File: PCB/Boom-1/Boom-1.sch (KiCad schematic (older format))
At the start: 714 parts, among them U1 CEM3340, U10 AS3320, U11 AS3310, U12 AS3310, U13 AS3310, U14 AS3310, U15 V2164D, U16 AS3310, U17 AS3310, U18 V2164D, U19 TL074, U2 CEM3340, U20 TL074, U21 TL074, U22 TL074, U23 TL074, U24 TL074, U25 TL074, U26 TL074, U27 TL072, U28 TL074, U29 TL072, U3 4013, U30 TL074, U31 TL072, U32 TL074, U33 TL074, U34 TL074, U35 TL072, U36 TL074, U37 TL074, U38 TL072, U39 TL074, U4 NOISE, U40 TL072, U5 V2164D, U6 V2164D, U7 V2164D, U8 AS3320, U9 AS3320

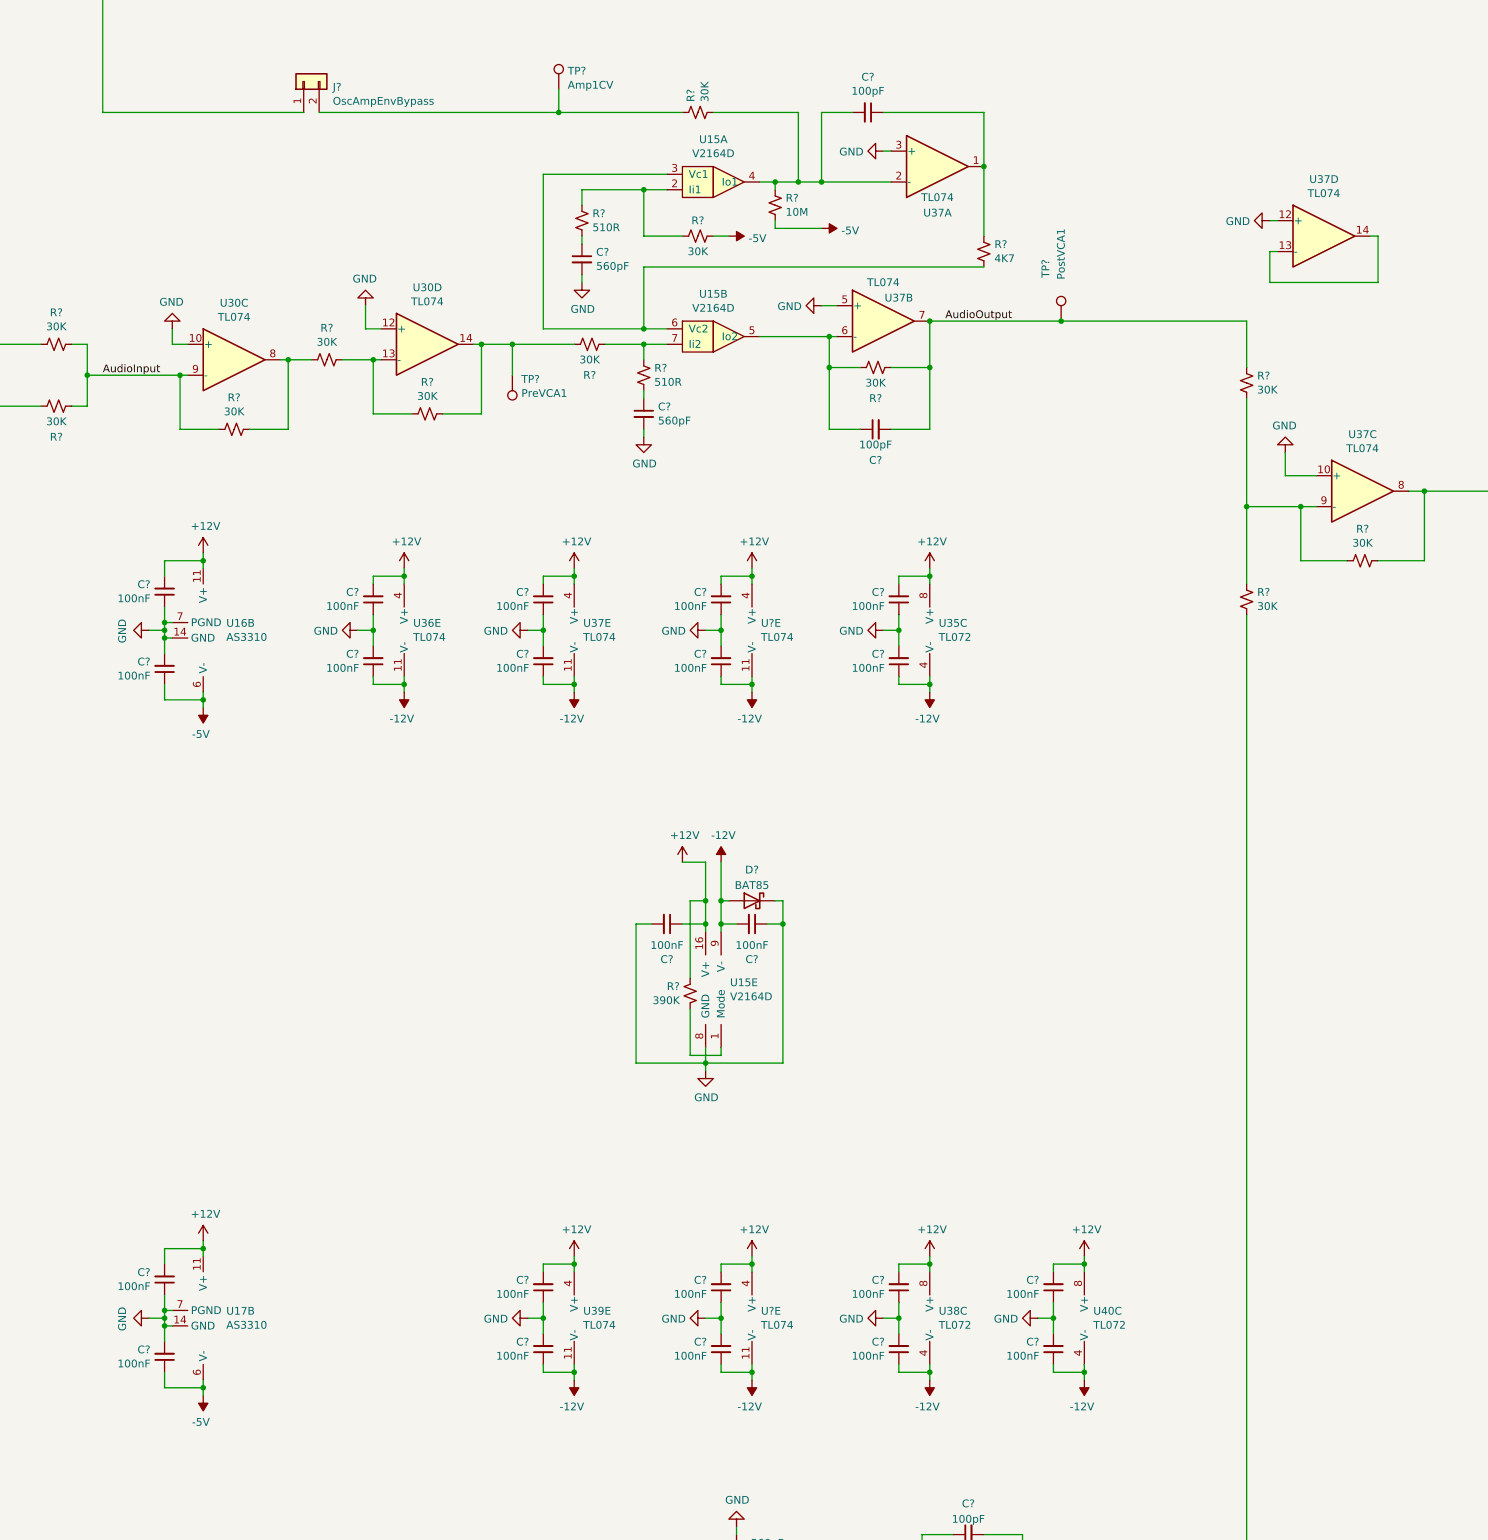
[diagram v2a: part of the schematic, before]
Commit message: removed unused power units from osc and sub amp and env column
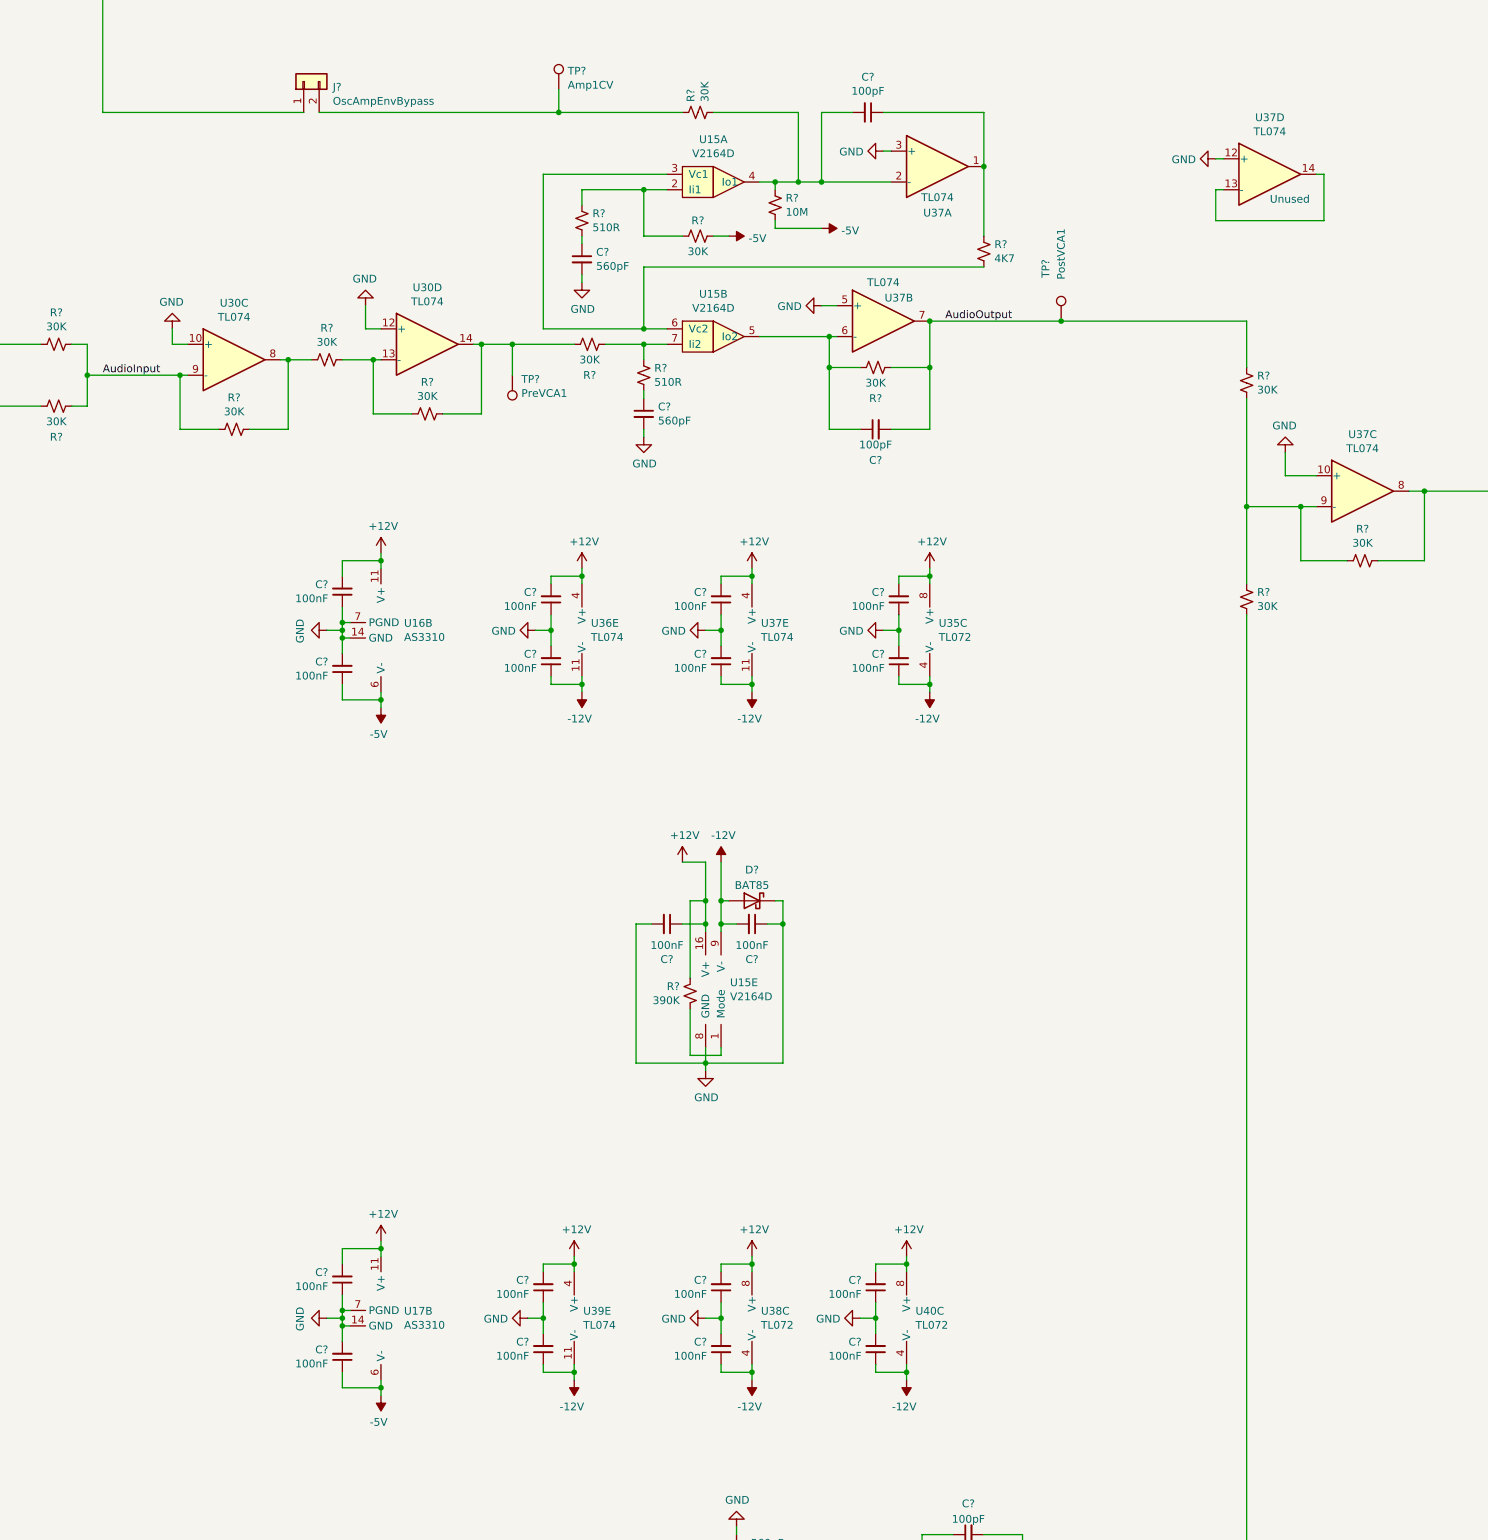
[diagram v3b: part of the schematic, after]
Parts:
- removed C? (x4): 100nF, symbol Device:C_Small
- removed U? (x2): TL074, symbol Amplifier_Operational:TL074
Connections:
- wire segments 3029 -> 3007
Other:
- note added: "Unused"
- moved on the sheet: C?, U16B, U17B, U36E, U37D, U37E, U38C, U40C

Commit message: U41, U42, U43, U44 are all TL074s in effects section
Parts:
- gave numbers to parts that had none: 4
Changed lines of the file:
@@
 $EndComp
 $Comp
-L Amplifier_Operational:TL074 U?
+L Amplifier_Operational:TL074 U41
 U 1 1 6218CA00
 P 43350 28750
-F 0 "U?" H 43450 29000 50  0000 C CNN
+F 0 "U41" H 43400 29000 50  0000 C CNN
 F 1 "TL074" H 43450 28900 50  0000 C CNN
 F 2 "" H 43300 28850 50  0001 C CNN
@@
 	43300 29250 43300 29350
 $Comp
-L Amplifier_Operational:TL074 U?
+L Amplifier_Operational:TL074 U41
 U 2 1 621954D3
 P 43000 29350
-F 0 "U?" H 43000 29717 50  0000 C CNN
-F 1 "TL074" H 43000 29626 50  0000 C CNN
+F 0 "U41" H 43000 29650 50  0000 C CNN
+F 1 "TL074" H 43000 29550 50  0000 C CNN
 F 2 "" H 42950 29450 50  0001 C CNN
 F 3 "http://www.ti.com/lit/ds/symlink/tl071.pdf" H 43050 29550 50  0001 C CNN
@@
 	43300 30400 43300 30750
 $Comp
-L Amplifier_Operational:TL074 U?
+L Amplifier_Operational:TL074 U41
 U 3 1 6219D961
 P 43000 30750
-F 0 "U?" H 43050 30900 50  0000 C CNN
+F 0 "U41" H 43050 30900 50  0000 C CNN
 F 1 "TL074" H 43000 31000 50  0000 C CNN
 F 2 "" H 42950 30850 50  0001 C CNN
@@
 	43300 30750 43300 30800
 $Comp
-L Amplifier_Operational:TL074 U?
+L Amplifier_Operational:TL074 U41
 U 4 1 621A56C4
 P 43350 31300
-F 0 "U?" H 43400 31550 50  0000 C CNN
+F 0 "U41" H 43400 31550 50  0000 C CNN
 F 1 "TL074" H 43450 31450 50  0000 C CNN
 F 2 "" H 43300 31400 50  0001 C CNN
@@
 Connection ~ 43050 31300
 $Comp
-L Amplifier_Operational:TL074 U?
+L Amplifier_Operational:TL074 U42
 U 1 1 621AF226
 P 44850 29250
-F 0 "U?" H 44850 29617 50  0000 C CNN
+F 0 "U42" H 44850 29617 50  0000 C CNN
 F 1 "TL074" H 44850 29526 50  0000 C CNN
 F 2 "" H 44800 29350 50  0001 C CNN
@@
 $EndComp
 $Comp
-L Amplifier_Operational:TL074 U?
+L Amplifier_Operational:TL074 U42
 U 2 1 621B7360
 P 44850 30450
-F 0 "U?" H 44850 30817 50  0000 C CNN
+F 0 "U42" H 44850 30817 50  0000 C CNN
 F 1 "TL074" H 44850 30726 50  0000 C CNN
 F 2 "" H 44800 30550 50  0001 C CNN
@@
 $EndComp
 $Comp
-L Amplifier_Operational:TL074 U?
+L Amplifier_Operational:TL074 U42
 U 3 1 621BF4FB
 P 46800 29150
-F 0 "U?" H 46800 29517 50  0000 C CNN
+F 0 "U42" H 46800 29517 50  0000 C CNN
 F 1 "TL074" H 46800 29426 50  0000 C CNN
 F 2 "" H 46750 29250 50  0001 C CNN
@@
 $EndComp
 $Comp
-L Amplifier_Operational:TL074 U?
+L Amplifier_Operational:TL074 U42
 U 4 1 621C6891
 P 46800 30350
-F 0 "U?" H 46800 30717 50  0000 C CNN
+F 0 "U42" H 46800 30717 50  0000 C CNN
 F 1 "TL074" H 46800 30626 50  0000 C CNN
 F 2 "" H 46750 30450 50  0001 C CNN
@@
 $EndComp
 $Comp
-L Amplifier_Operational:TL074 U?
+L Amplifier_Operational:TL074 U43
 U 1 1 621CEC11
 P 48350 26300
-F 0 "U?" H 48350 26667 50  0000 C CNN
+F 0 "U43" H 48350 26667 50  0000 C CNN
 F 1 "TL074" H 48350 26576 50  0000 C CNN
 F 2 "" H 48300 26400 50  0001 C CNN
@@
 $EndComp
 $Comp
-L Amplifier_Operational:TL074 U?
+L Amplifier_Operational:TL074 U43
 U 2 1 621D8411
 P 50900 26300
-F 0 "U?" H 50900 26667 50  0000 C CNN
+F 0 "U43" H 50900 26667 50  0000 C CNN
 F 1 "TL074" H 50900 26576 50  0000 C CNN
 F 2 "" H 50850 26400 50  0001 C CNN
@@
 $EndComp
 $Comp
-L Amplifier_Operational:TL074 U?
+L Amplifier_Operational:TL074 U43
 U 3 1 621DFEFF
 P 51100 29350
-F 0 "U?" H 51100 29717 50  0000 C CNN
+F 0 "U43" H 51100 29717 50  0000 C CNN
 F 1 "TL074" H 51100 29626 50  0000 C CNN
 F 2 "" H 51050 29450 50  0001 C CNN
@@
 $EndComp
 $Comp
-L Amplifier_Operational:TL074 U?
+L Amplifier_Operational:TL074 U43
 U 4 1 621E86F4
 P 51100 30550
-F 0 "U?" H 51100 30917 50  0000 C CNN
+F 0 "U43" H 51100 30917 50  0000 C CNN
 F 1 "TL074" H 51100 30826 50  0000 C CNN
 F 2 "" H 51050 30650 50  0001 C CNN
@@
 $EndComp
 $Comp
-L Amplifier_Operational:TL074 U?
+L Amplifier_Operational:TL074 U44
 U 1 1 621EF914
 P 55100 29200
-F 0 "U?" H 55100 29567 50  0000 C CNN
+F 0 "U44" H 55100 29567 50  0000 C CNN
 F 1 "TL074" H 55100 29476 50  0000 C CNN
 F 2 "" H 55050 29300 50  0001 C CNN
@@
 Connection ~ 55400 29200
 $Comp
-L Amplifier_Operational:TL074 U?
+L Amplifier_Operational:TL074 U44
 U 2 1 621F74C9
 P 55100 30400
-F 0 "U?" H 55100 30767 50  0000 C CNN
+F 0 "U44" H 55100 30767 50  0000 C CNN
 F 1 "TL074" H 55100 30676 50  0000 C CNN
 F 2 "" H 55050 30500 50  0001 C CNN
@@
 Connection ~ 55400 30400
 $Comp
-L Amplifier_Operational:TL074 U?
+L Amplifier_Operational:TL074 U44
 U 3 1 621FEFE1
 P 56700 29100
-F 0 "U?" H 56700 29467 50  0000 C CNN
+F 0 "U44" H 56700 29467 50  0000 C CNN
 F 1 "TL074" H 56700 29376 50  0000 C CNN
 F 2 "" H 56650 29200 50  0001 C CNN
@@
 Connection ~ 57000 29100
 $Comp
-L Amplifier_Operational:TL074 U?
+L Amplifier_Operational:TL074 U44
 U 4 1 6220712E
 P 56700 30300
-F 0 "U?" H 56700 30667 50  0000 C CNN
+F 0 "U44" H 56700 30667 50  0000 C CNN
 F 1 "TL074" H 56700 30576 50  0000 C CNN
 F 2 "" H 56650 30400 50  0001 C CNN
@@
 	32950 35750 32950 35800
 $Comp
-L Amplifier_Operational:TL074 U?
+L Amplifier_Operational:TL074 U44
 U 5 1 7BA24959
 P 49300 33700
-F 0 "U?" H 49258 33746 50  0000 L CNN
+F 0 "U44" H 49258 33746 50  0000 L CNN
 F 1 "TL074" H 49258 33655 50  0000 L CNN
 F 2 "" H 49250 33800 50  0001 C CNN
@@
 	49200 34050 49200 34100
 $Comp
-L Amplifier_Operational:TL074 U?
+L Amplifier_Operational:TL074 U43
 U 5 1 7BA24A33
 P 48150 33700
-F 0 "U?" H 48108 33746 50  0000 L CNN
+F 0 "U43" H 48108 33746 50  0000 L CNN
 F 1 "TL074" H 48108 33655 50  0000 L CNN
 F 2 "" H 48100 33800 50  0001 C CNN
@@
 	48050 34050 48050 34100
 $Comp
-L Amplifier_Operational:TL074 U?
+L Amplifier_Operational:TL074 U42
 U 5 1 7BA24B0D
 P 47050 33700
-F 0 "U?" H 47008 33746 50  0000 L CNN
+F 0 "U42" H 47008 33746 50  0000 L CNN
 F 1 "TL074" H 47008 33655 50  0000 L CNN
 F 2 "" H 47000 33800 50  0001 C CNN
@@
 	46950 34050 46950 34100
 $Comp
-L Amplifier_Operational:TL074 U?
+L Amplifier_Operational:TL074 U41
 U 5 1 7C27EEA1
 P 45900 33700
-F 0 "U?" H 45858 33746 50  0000 L CNN
+F 0 "U41" H 45858 33746 50  0000 L CNN
 F 1 "TL074" H 45858 33655 50  0000 L CNN
 F 2 "" H 45850 33800 50  0001 C CNN

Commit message: U45 and U46 are power regulators
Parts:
- gave numbers to parts that had none: 2
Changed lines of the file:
@@
 Connection ~ 11000 15700
 $Comp
-L Regulator_Linear:L7905 U?
+L Regulator_Linear:L7905 U45
 U 1 1 8F2A5DBC
 P 49600 11750
-F 0 "U?" H 49600 11508 50  0000 C CNN
+F 0 "U45" H 49600 11508 50  0000 C CNN
 F 1 "L7905" H 49600 11599 50  0000 C CNN
 F 2 "" H 49600 11550 50  0001 C CIN
@@
 $EndComp
 $Comp
-L Regulator_Linear:L7805 U?
+L Regulator_Linear:L7805 U46
 U 1 1 8F2AF784
 P 51200 11750
-F 0 "U?" H 51200 11992 50  0000 C CNN
+F 0 "U46" H 51200 11992 50  0000 C CNN
 F 1 "L7805" H 51200 11901 50  0000 C CNN
 F 2 "" H 51225 11600 50  0001 L CIN

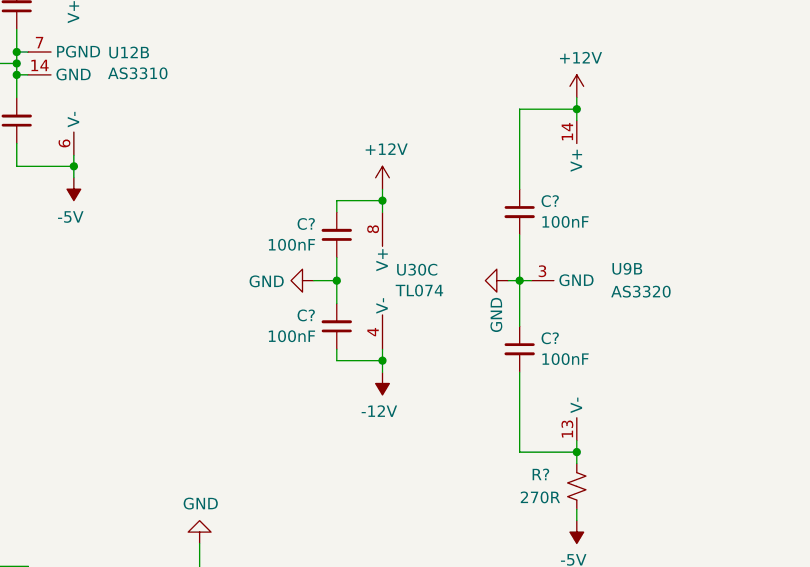
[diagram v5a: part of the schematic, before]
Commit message: Fixed U30 power unit, was TL072 shoudl be TL074
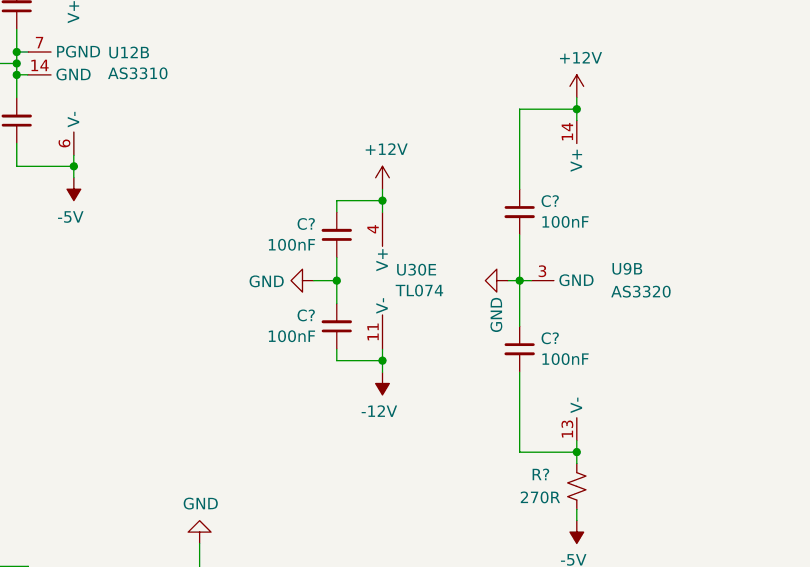
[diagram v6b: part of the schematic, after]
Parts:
- removed U30: TL074, symbol Amplifier_Operational:TL072
- added unit 5 of U30
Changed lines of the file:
@@
 	24050 27800 24050 27850
 $Comp
-L Amplifier_Operational:TL072 U30
-U 3 1 74BE356E
-P 26550 29100
-F 0 "U30" H 26508 29146 50  0000 L CNN
-F 1 "TL074" H 26508 29055 50  0000 L CNN
-F 2 "" H 26550 29100 50  0001 C CNN
-F 3 "http://www.ti.com/lit/ds/symlink/tl071.pdf" H 26550 29100 50  0001 C CNN
-	3    26550 29100
-	1    0    0    -1
-$EndComp
-$Comp
 L power:GND #PWR?
 U 1 1 74BE360C
@@
 Text Notes 37450 28200 0    50   ~ 0
 Unused
+$Comp
+L Amplifier_Operational:TL074 U30
+U 5 1 6DB68DCC
+P 26550 29100
+F 0 "U30" H 26508 29146 50  0000 L CNN
+F 1 "TL074" H 26508 29055 50  0000 L CNN
+F 2 "" H 26500 29200 50  0001 C CNN
+F 3 "http://www.ti.com/lit/ds/symlink/tl071.pdf" H 26600 29300 50  0001 C CNN
+	5    26550 29100
+	1    0    0    -1
+$EndComp
 $EndSCHEMATC

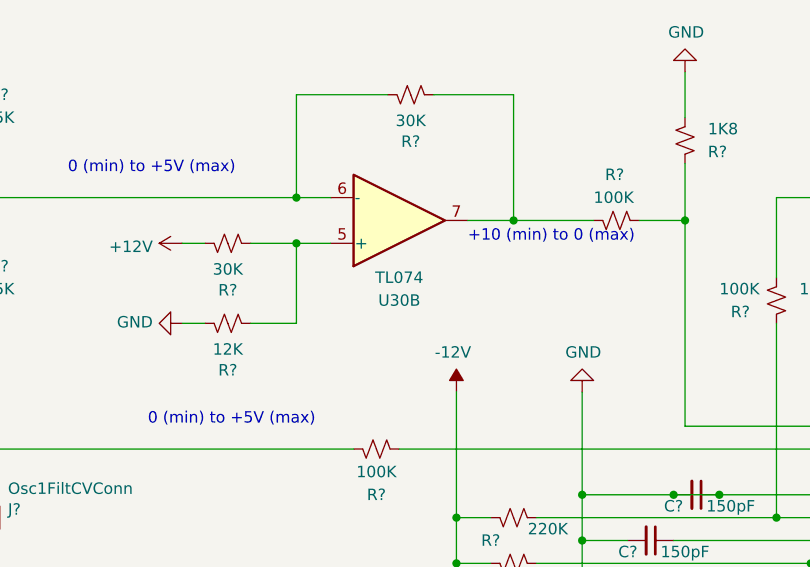
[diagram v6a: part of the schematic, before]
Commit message: Fixed U30 units A and B, were TL072 should be TL074
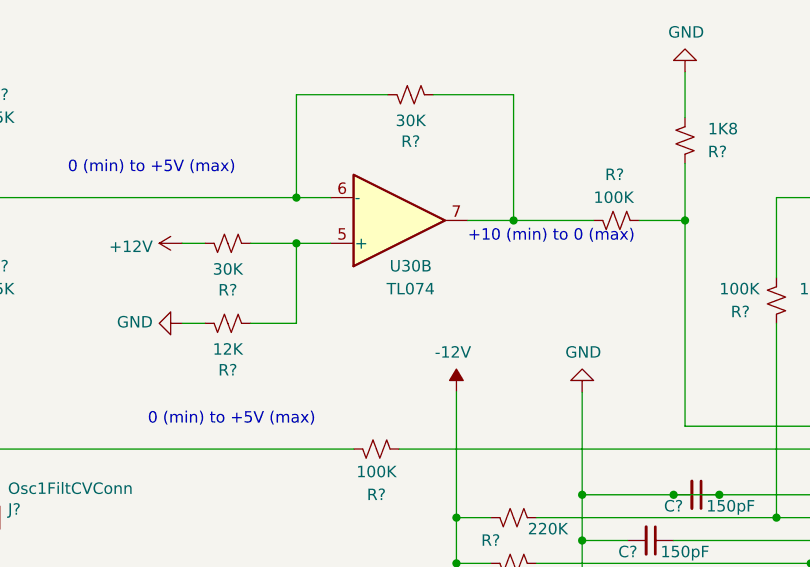
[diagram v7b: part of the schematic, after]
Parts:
- removed unit 1 of U30
- removed unit 2 of U30
- added unit 1 of U30
- added unit 2 of U30
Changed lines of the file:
@@
 $EndComp
 $Comp
-L Amplifier_Operational:TL072 U30
-U 1 1 60766DB9
-P 21550 31600
-F 0 "U30" H 21550 31967 50  0000 C CNN
-F 1 "TL074" H 21550 31876 50  0000 C CNN
-F 2 "" H 21550 31600 50  0001 C CNN
-F 3 "http://www.ti.com/lit/ds/symlink/tl071.pdf" H 21550 31600 50  0001 C CNN
-	1    21550 31600
-	1    0    0    -1
-$EndComp
-Connection ~ 21850 31600
-$Comp
-L Amplifier_Operational:TL072 U30
-U 2 1 60771100
-P 24400 30900
-F 0 "U30" H 24400 31250 50  0000 C CNN
-F 1 "TL074" H 24400 31150 50  0000 C CNN
-F 2 "" H 24400 30900 50  0001 C CNN
-F 3 "http://www.ti.com/lit/ds/symlink/tl071.pdf" H 24400 30900 50  0001 C CNN
-	2    24400 30900
-	1    0    0    1
-$EndComp
-$Comp
 L Amplifier_Operational:TL074 U41
 U 1 1 6218CA00
@@
 	1    0    0    -1
 $EndComp
+$Comp
+L Amplifier_Operational:TL074 U30
+U 1 1 6E4EB8FA
+P 21550 31600
+F 0 "U30" H 21550 31967 50  0000 C CNN
+F 1 "TL074" H 21550 31876 50  0000 C CNN
+F 2 "" H 21500 31700 50  0001 C CNN
+F 3 "http://www.ti.com/lit/ds/symlink/tl071.pdf" H 21600 31800 50  0001 C CNN
+	1    21550 31600
+	1    0    0    -1
+$EndComp
+Connection ~ 21850 31600
+$Comp
+L Amplifier_Operational:TL074 U30
+U 2 1 6E4F472D
+P 24400 30900
+F 0 "U30" H 24450 31100 50  0000 C CNN
+F 1 "TL074" H 24450 31200 50  0000 C CNN
+F 2 "" H 24350 31000 50  0001 C CNN
+F 3 "http://www.ti.com/lit/ds/symlink/tl071.pdf" H 24450 31100 50  0001 C CNN
+	2    24400 30900
+	1    0    0    1
+$EndComp
 $EndSCHEMATC

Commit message: Applied automatic annotation, no errors
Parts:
- gave numbers to parts that had none: 646
